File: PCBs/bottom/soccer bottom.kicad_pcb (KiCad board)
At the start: 2 copper layers, 90 x 90 mm, 52 parts, among them J1 Conn_01x04_Socket, J2 Conn_01x03_Socket, U1 CD74HC4067SM, U10 QRE1113GR, U11 QRE1113GR, U12 QRE1113GR, U13 QRE1113GR, U14 QRE1113GR, U15 QRE1113GR, U16 QRE1113GR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

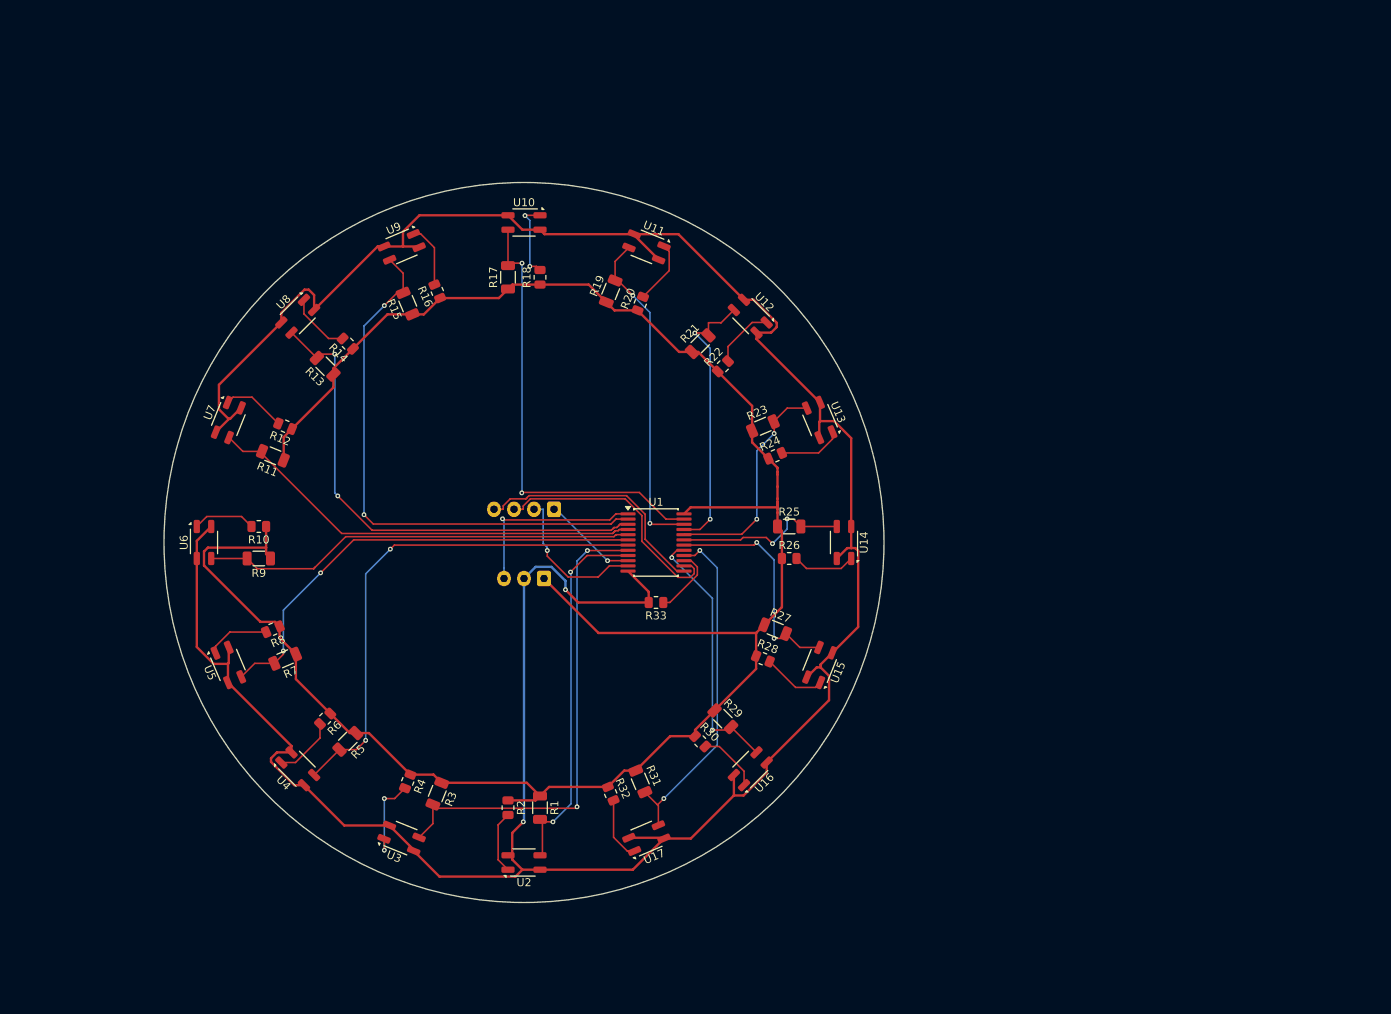
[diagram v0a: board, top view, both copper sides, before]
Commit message: NEW MCU
rp2040-zero and mosfets

grr haven't made the pcb
schematic is good tho!
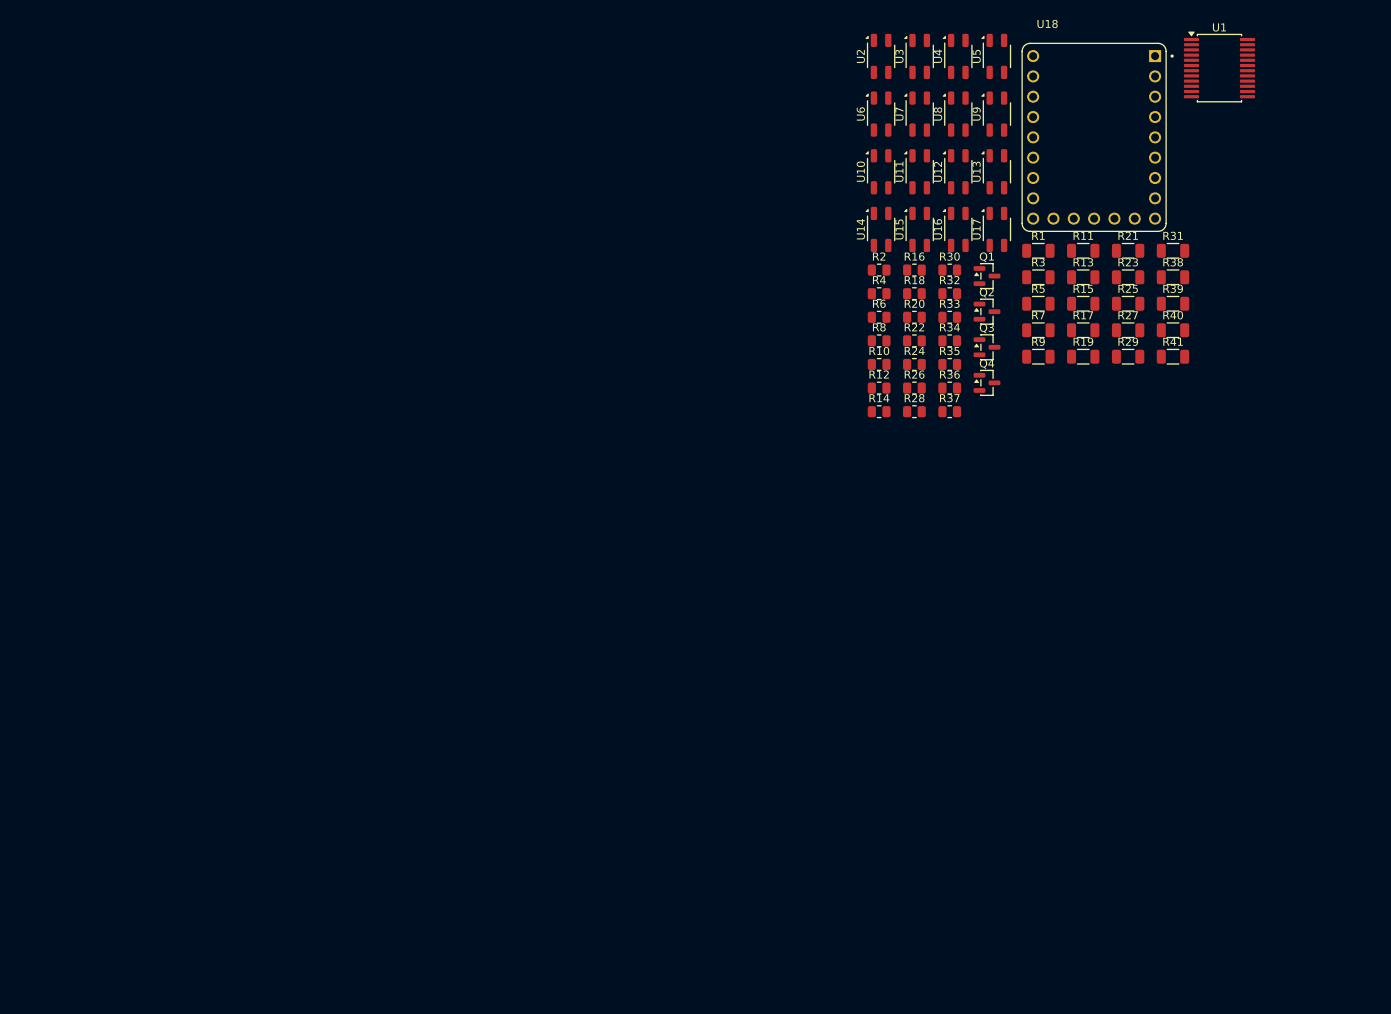
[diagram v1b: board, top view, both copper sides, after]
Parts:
- removed J1: Conn_01x04_Socket, Connector_JST:JST_XH_B4B-XH-A_1x04_P2.50mm_Vertical
- removed J2: Conn_01x03_Socket, Connector_JST:JST_XH_B3B-XH-A_1x03_P2.50mm_Vertical
- added Q1: AO3400A, Package_TO_SOT_SMD:SOT-23, F.Cu at (157.9, 66.7)
- added Q2: AO3400A, Package_TO_SOT_SMD:SOT-23, F.Cu at (157.9, 71.1)
- added Q3: AO3400A, Package_TO_SOT_SMD:SOT-23, F.Cu at (157.9, 75.6)
- added Q4: AO3400A, Package_TO_SOT_SMD:SOT-23, F.Cu at (157.9, 80.0)
- added R34: 100k, Resistor_SMD:R_0805_2012Metric, F.Cu at (153.2, 74.8)
- added R35: 100k, Resistor_SMD:R_0805_2012Metric, F.Cu at (153.2, 77.7)
- added R36: 100k, Resistor_SMD:R_0805_2012Metric, F.Cu at (153.2, 80.7)
- added R37: 100k, Resistor_SMD:R_0805_2012Metric, F.Cu at (153.2, 83.6)
- added R38: 100, Resistor_SMD:R_1206_3216Metric, F.Cu at (181.1, 66.8)
- added R39: 100, Resistor_SMD:R_1206_3216Metric, F.Cu at (181.1, 70.2)
- added R40: 100, Resistor_SMD:R_1206_3216Metric, F.Cu at (181.1, 73.5)
- added R41: 100, Resistor_SMD:R_1206_3216Metric, F.Cu at (181.1, 76.8)
- added U18: RP2040-ZERO, RP2040-ZERO:MODULE_RP2040-ZERO, F.Cu at (171.3, 49.4)
- moved U5 122.5 mm to (159.1, 39.2), turned to 0 degrees
- moved U4 121.4 mm to (154.3, 39.2), turned to 0 degrees
- moved U3 117.2 mm to (149.5, 39.2), turned to 0 degrees
- moved U2 110.2 mm to (144.6, 39.2), turned to 0 degrees
- moved R11 104.5 mm to (169.9, 63.5), turned to 0 degrees
- moved R7 102.7 mm to (164.3, 73.5), turned to 0 degrees
- moved R5 102.2 mm to (164.3, 70.2), turned to 0 degrees
- moved R9 100.7 mm to (164.3, 76.8), turned to 0 degrees
- moved U6 100.2 mm to (144.6, 46.4)
- moved R3 99.1 mm to (164.3, 66.8), turned to 0 degrees
- moved R13 95.4 mm to (169.9, 66.8), turned to 0 degrees
- moved U7 94.5 mm to (149.5, 46.4), turned to 0 degrees
- moved R31 94.0 mm to (181.1, 63.5), turned to 0 degrees
- moved R1 93.4 mm to (164.3, 63.5), turned to 0 degrees
- moved U1 92.1 mm to (186.9, 40.7)
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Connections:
- U10 pad 2: GND -> /GND_3
- U10 pad 4: GND -> /GND_3
- U11 pad 2: GND -> /GND_3
- U11 pad 4: GND -> /GND_3
- U12 pad 2: GND -> /GND_3
- U12 pad 4: GND -> /GND_3
- U13 pad 2: GND -> /GND_3
- U13 pad 4: GND -> /GND_3
- U14 pad 2: GND -> /GND_4
- U14 pad 4: GND -> /GND_4
- U15 pad 2: GND -> /GND_4
- U15 pad 4: GND -> /GND_4
- U16 pad 2: GND -> /GND_4
- U16 pad 4: GND -> /GND_4
- U17 pad 2: GND -> /GND_4
- U17 pad 4: GND -> /GND_4
- U2 pad 2: GND -> /GND_1
- U2 pad 4: GND -> /GND_1
- U3 pad 2: GND -> /GND_1
- U3 pad 4: GND -> /GND_1
- U4 pad 2: GND -> /GND_1
- U4 pad 4: GND -> /GND_1
- U5 pad 2: GND -> /GND_1
- U5 pad 4: GND -> /GND_1
- U6 pad 2: GND -> /GND_2
- U6 pad 4: GND -> /GND_2
- U7 pad 2: GND -> /GND_2
- U7 pad 4: GND -> /GND_2
- U8 pad 2: GND -> /GND_2
- U8 pad 4: GND -> /GND_2
- U9 pad 2: GND -> /GND_2
- U9 pad 4: GND -> /GND_2
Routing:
- net GND: track 364.4 -> 0.00 mm, vias 2 -> 0
- net +5V: track 262.9 -> 0.00 mm
- net /ir_7: track 68.8 -> 0.00 mm, vias 2 -> 0
- net /ir_6: track 63.6 -> 0.00 mm, vias 2 -> 0
- net /ir_2: track 63.3 -> 0.00 mm, vias 2 -> 0
- net /ir_1: track 60.8 -> 0.00 mm, vias 2 -> 0
- net /ir_3: track 58.7 -> 0.00 mm, vias 2 -> 0
- net /ir_8: track 56.8 -> 0.00 mm, vias 2 -> 0
- net /ir_5: track 55.5 -> 0.00 mm
- net /ir_4: track 54.7 -> 0.00 mm
- net /ir_0: track 46.3 -> 0.00 mm, vias 2 -> 0
- net /ir_15: track 42.9 -> 0.00 mm, vias 2 -> 0
- net /ir_9: track 42.0 -> 0.00 mm, vias 2 -> 0
- net /ir_10: track 36.1 -> 0.00 mm, vias 2 -> 0
- net /ir_14: track 32.7 -> 0.00 mm, vias 2 -> 0
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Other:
- board outline removed

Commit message: v2.1
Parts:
- added J1: Conn_01x04_Socket, Connector_JST:JST_XH_B4B-XH-A_1x04_P2.50mm_Vertical, F.Cu at (196.2, 55.4)
- R34, R35, R36, R37: value 100k -> 10k
- moved U14 95.6 mm to (166.2, 154.0)
- moved U15 95.6 mm to (171.1, 154.0)
- moved U16 95.6 mm to (175.9, 154.0)
- moved U17 95.6 mm to (180.7, 154.0)
- moved R30 86.1 mm to (175.9, 149.0)
- moved R32 84.9 mm to (181.3, 149.0)
- moved R31 82.0 mm to (182.3, 145.5)
- moved U10 80.3 mm to (164.2, 131.5)
- moved U11 80.3 mm to (169.1, 131.5)
- moved U12 80.3 mm to (173.9, 131.5)
- moved U13 80.3 mm to (178.7, 131.5)
- moved R41 79.8 mm to (190.8, 156.0)
- moved R37 78.8 mm to (185.1, 155.7)
- moved Q4 77.8 mm to (186.3, 152.4)
- moved R25 75.8 mm to (166.9, 145.5)
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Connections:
- U18 pad 13: unconnected-(U18-GP12-Pad13) -> /SDA
- U18 pad 14: unconnected-(U18-GP13-Pad14) -> /SCL
- U18 pad 22: unconnected-(U18-GND-Pad22) -> GND
- U18 pad 23: unconnected-(U18-5V-Pad23) -> +5V

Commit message: bottom pcb update
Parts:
- added C1: 100n, Capacitor_SMD:C_0805_2012Metric, F.Cu at (186.0, 66.2)
- added R42: 3.3k, Resistor_SMD:R_0805_2012Metric, F.Cu at (165.2, 74.9)
- added R43: 3.3k, Resistor_SMD:R_0805_2012Metric, F.Cu at (165.2, 77.9)
- R1, R11, R13, R15, R17, R19, R21, R23, R25, R27, R29, R3, R31, R5, R7, R9: value 100 -> 10k; footprint Resistor_SMD:R_1206_3216Metric -> Resistor_SMD:R_0805_2012Metric
- R10, R12, R14, R16, R18, R2, R20, R22, R24, R26, R28, R30, R32, R4, R6, R8: value 10k -> 100
- R38, R39, R40, R41: footprint Resistor_SMD:R_1206_3216Metric -> Resistor_SMD:R_0805_2012Metric
- moved R1 0.92 mm to (162.0, 84.8)
- moved R2 0.86 mm to (161.6, 88.5)
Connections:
- U18 pad 21: unconnected-(U18-3V3-Pad21) -> Net-(U18-3V3)

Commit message: bottom v2 (pcb)
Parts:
- removed the Q4 at (186.3, 152.4)
- removed the R31 at (182.3, 145.5)
- removed the R32 at (181.3, 149.0)
- removed the R37 at (185.1, 155.7)
- removed the R41 at (190.8, 156.0)
- removed the U17 at (180.7, 154.0)
- added C2: 100n, Capacitor_SMD:C_0805_2012Metric, F.Cu at (83.5, 87.5)
- added C3: 10u, Capacitor_SMD:C_0805_2012Metric, F.Cu at (83.5, 85.0)
- added C4: 100n, Capacitor_SMD:C_0805_2012Metric, F.Cu at (83.5, 97.5)
- added C5: 10u, Capacitor_SMD:C_0805_2012Metric, F.Cu at (83.5, 100.0)
- added Q1: AO3400A, Package_TO_SOT_SMD:SOT-23, F.Cu at (123.5, 76.5)
- added R1: 10k, Resistor_SMD:R_0805_2012Metric, F.Cu at (137.5, 98.0)
- added R2: 100, Resistor_SMD:R_0805_2012Metric, F.Cu at (137.5, 102.0)
- added R34: 10k, Resistor_SMD:R_0805_2012Metric, F.Cu at (119.0, 78.0)
- added R38: 100, Resistor_SMD:R_0805_2012Metric, F.Cu at (120.5, 79.5)
- added REF**: MountingHole_3.2mm_M3_DIN965_Pad, MountingHole:MountingHole_3.2mm_M3_DIN965_Pad, F.Cu at (122.2, 133.3)
- added REF**: MountingHole_3.2mm_M3_DIN965_Pad, MountingHole:MountingHole_3.2mm_M3_DIN965_Pad, F.Cu at (66.7, 122.2)
- added REF**: MountingHole_3.2mm_M3_DIN965_Pad, MountingHole:MountingHole_3.2mm_M3_DIN965_Pad, F.Cu at (77.8, 66.7)
- added REF**1: MountingHole_3.2mm_M3_DIN965_Pad, MountingHole:MountingHole_3.2mm_M3_DIN965_Pad, F.Cu at (133.3, 77.8)
- added U19: AMS1117-3.3, Package_TO_SOT_SMD:SOT-223-3_TabPin2, F.Cu at (83.5, 92.5)
- added U2: QRE1113GR, OptoDevice:OnSemi_CASE100CY, F.Cu at (141.5, 100.0)
- J1: moved to B.Cu
- U18: footprint RP2040-ZERO:MODULE_RP2040-ZERO -> Footprints:MODULE_RP2040-ZERO; moved to B.Cu
- moved U9 119.2 mm to (61.7, 84.1), turned to -22.5 degrees
- moved R15 116.4 mm to (64.6, 87.5), turned to 157.5 degrees
- moved R39 115.7 mm to (79.5, 79.5), turned to 135 degrees
- moved R16 115.2 mm to (66.1, 83.8), turned to 157.5 degrees
- moved R35 114.2 mm to (78.0, 81.0), turned to -45 degrees
- moved R40 113.0 mm to (79.5, 120.5), turned to -135 degrees
- moved Q2 112.6 mm to (76.5, 76.5), turned to 135 degrees
- moved U10 110.3 mm to (58.5, 100.0)
- moved U8 110.3 mm to (70.7, 70.7), turned to -45 degrees
- moved Q3 110.2 mm to (76.5, 123.5), turned to -135 degrees
- moved R36 109.3 mm to (81.0, 122.0), turned to 45 degrees
- moved U11 108.5 mm to (61.7, 115.9), turned to 22.5 degrees
- moved R18 106.3 mm to (62.5, 98.0), turned to 180 degrees
- moved R13 106.1 mm to (72.1, 74.9), turned to 135 degrees
- moved R20 105.4 mm to (64.6, 112.5), turned to -157.5 degrees
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- renumbered Q1 to Q4, R1 to R31, R2 to R32, R34 to R37, R38 to R41, U2 to U17
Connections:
- C1 pad 1: +5V -> +3.3V
- J1 pad 1: /SDA -> /SCL
- J1 pad 2: /SCL -> /SDA
- J1 pad 3: +5V -> GND
- J1 pad 4: GND -> +5V
- Q4 pad 3: /GND_1 -> /GND_4
- R10 pad 1: +5V -> +3.3V
- R11 pad 1: +5V -> +3.3V
- R12 pad 1: +5V -> +3.3V
- R13 pad 1: +5V -> +3.3V
- R14 pad 1: +5V -> +3.3V
- R15 pad 1: +5V -> +3.3V
- R16 pad 1: +5V -> +3.3V
- R17 pad 1: +5V -> +3.3V
- R18 pad 1: +5V -> +3.3V
- R19 pad 1: +5V -> +3.3V
- R20 pad 1: +5V -> +3.3V
- R21 pad 1: +5V -> +3.3V
- R22 pad 1: +5V -> +3.3V
- R23 pad 1: +5V -> +3.3V
- R24 pad 1: +5V -> +3.3V
- R25 pad 1: +5V -> +3.3V
- R26 pad 1: +5V -> +3.3V
- R27 pad 1: +5V -> +3.3V
- R28 pad 1: +5V -> +3.3V
- R29 pad 1: +5V -> +3.3V
- R3 pad 1: +5V -> +3.3V
- R30 pad 1: +5V -> +3.3V
- R31 pad 1: +5V -> +3.3V
- R31 pad 2: /ir_0 -> /ir_15
- R32 pad 1: +5V -> +3.3V
- R4 pad 1: +5V -> +3.3V
- R41 pad 1: Net-(U18-GP6) -> Net-(U18-GP9)
- R42 pad 1: Net-(U18-3V3) -> +3.3V
- R43 pad 1: Net-(U18-3V3) -> +3.3V
- R5 pad 1: +5V -> +3.3V
- R6 pad 1: +5V -> +3.3V
- R7 pad 1: +5V -> +3.3V
- R8 pad 1: +5V -> +3.3V
- R9 pad 1: +5V -> +3.3V
- U1 pad 16: /ir_15 -> /ir_8
- U1 pad 17: /ir_14 -> /ir_9
- U1 pad 18: /ir_13 -> /ir_10
- U1 pad 19: /ir_12 -> /ir_11
- U1 pad 20: /ir_11 -> /ir_12
- U1 pad 21: /ir_10 -> /ir_13
- U1 pad 22: /ir_9 -> /ir_14
- U1 pad 23: /ir_8 -> /ir_15
- U1 pad 24: +5V -> +3.3V
- U17 pad 2: /GND_1 -> /GND_4
- U17 pad 3: /ir_0 -> /ir_15
- U17 pad 4: /GND_1 -> /GND_4
- U18 pad 21: Net-(U18-3V3) -> +3.3V
- U18 pad 23: +5V -> unconnected-(U18-5V-Pad23)
- U18 pad 3: Net-(U1-S0) -> Net-(U1-S1)
- U18 pad 4: Net-(U1-S1) -> Net-(U1-S0)
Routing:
- net /ir_4: track 0.00 -> 110.2 mm, vias 0 -> 2
- net /ir_5: track 0.00 -> 99.2 mm, vias 0 -> 2
- net /GND_2: track 0.00 -> 90.6 mm
- net /GND_4: track 0.00 -> 90.6 mm
- net /GND_3: track 0.00 -> 90.6 mm
- net /GND_1: track 0.00 -> 90.6 mm
- net /ir_6: track 0.00 -> 86.7 mm, vias 0 -> 2
- net /ir_9: track 0.00 -> 76.7 mm
- net /ir_8: track 0.00 -> 75.3 mm
- net /ir_10: track 0.00 -> 74.0 mm
- net /ir_11: track 0.00 -> 71.2 mm
- net +3.3V: track 0.00 -> 70.8 mm, vias 0 -> 51
- net /ir_7: track 0.00 -> 70.5 mm
- net /ir_12: track 0.00 -> 68.0 mm
- net /ir_13: track 0.00 -> 56.6 mm
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- added copper zone on F.Cu, net +3.3V
- added copper zone on In1.Cu, net +3.3V
- added copper zone on B.Cu, net GND
- added copper zone on F.Cu, net GND
- added copper zone on In2.Cu, net GND
- added copper zone on F.Cu, net Net-(Q1-G)
- added copper zone on F.Cu, net Net-(Q2-G)
- added copper zone on F.Cu, net Net-(Q3-G)
- added copper zone on F.Cu, net Net-(Q4-G)
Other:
- board outline added: 90 x 90 mm
- copper layers 2 -> 4

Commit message: bottom align
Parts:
- turned J1 to 168.75 degrees
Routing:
- net GND: track 20.0 -> 17.6 mm, vias 86 -> 89
- net +5V: track 23.7 -> 25.2 mm
- net /ir_3: track 41.5 -> 40.3 mm, vias 1 -> 0
- net Net-(U1-S3): vias 2 -> 1
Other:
- board text added: "MINDSTORMERS bottom PCB 16x QRE1113GR IR reflectance sensors designed by aiden"
